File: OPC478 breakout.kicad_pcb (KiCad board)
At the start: 2 copper layers, 26 x 29.8 mm, 14 parts, among them J1 Conn_01x05_Pin, J2 AudioPlug4, Q1 BC557, Q2 BC547

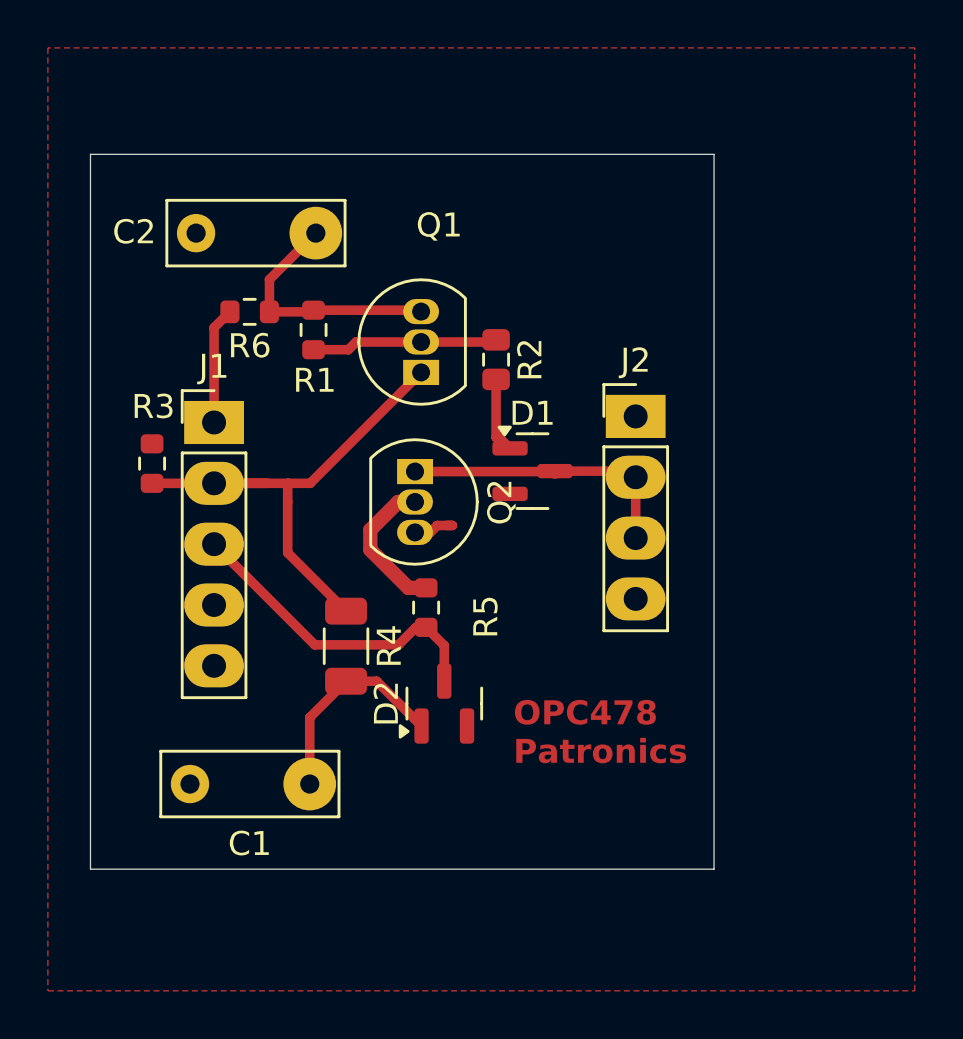
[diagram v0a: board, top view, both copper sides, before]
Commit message: adjust component layers to better match physical assembly
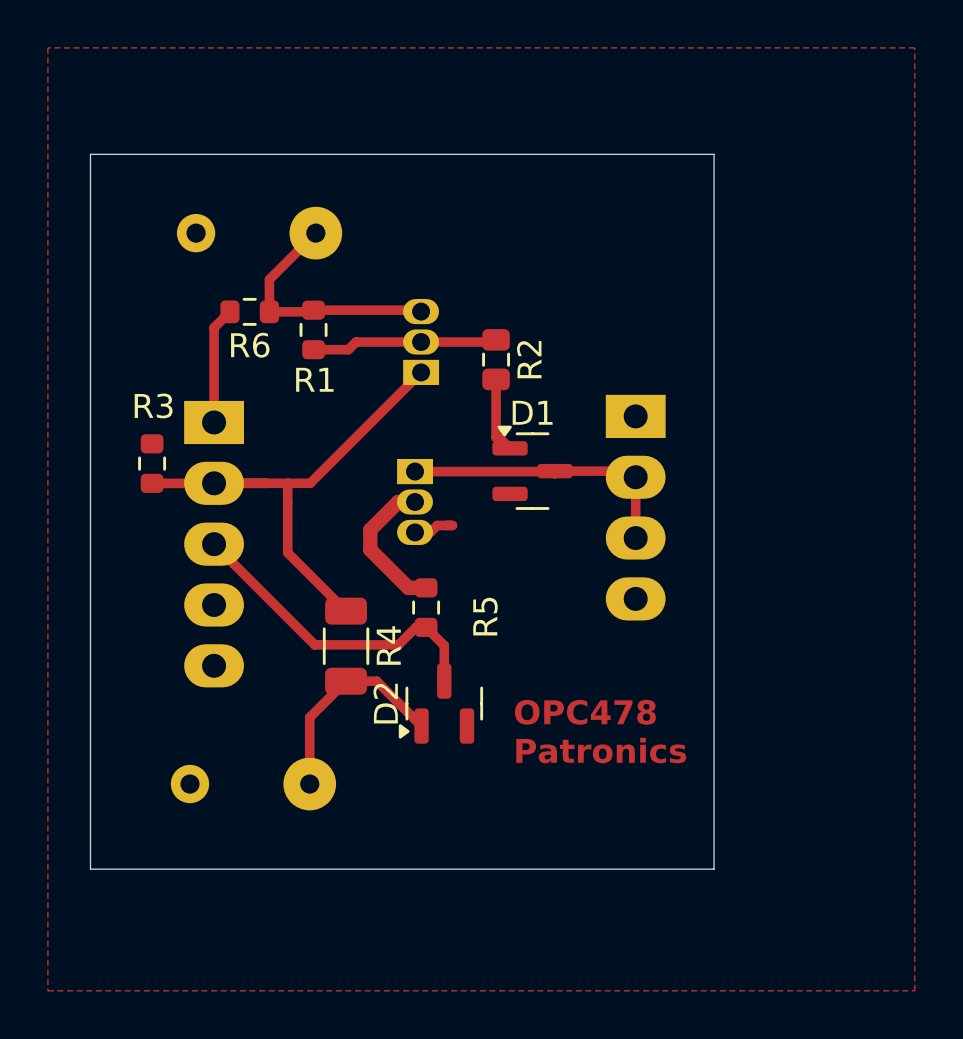
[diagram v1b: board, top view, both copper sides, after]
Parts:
- C1, C2, J1, J2, Q1, Q2: moved to B.Cu
- turned J1 to 180 degrees
- turned J2 to 180 degrees

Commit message: further widen pads and traces to improve ease of milling and soldering
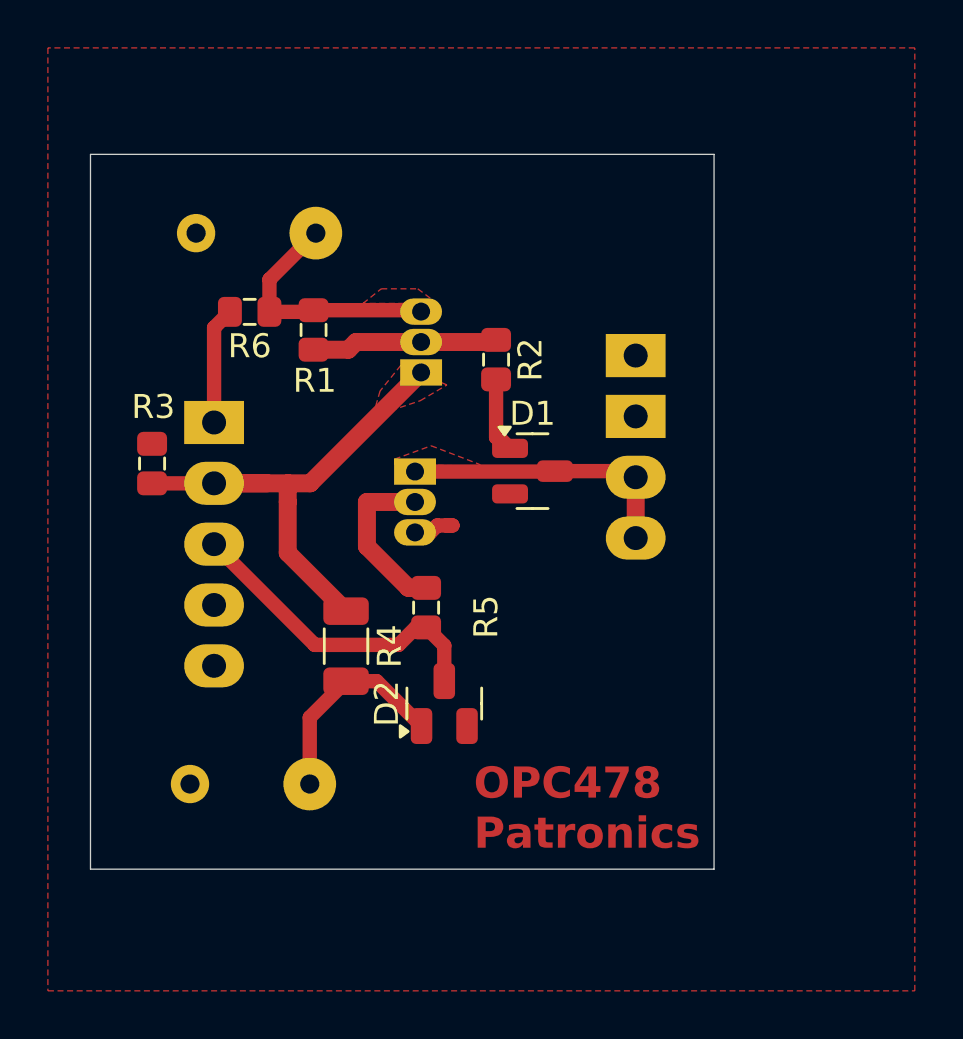
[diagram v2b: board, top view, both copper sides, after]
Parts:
- moved J2 2.54 mm to (121.8, 76.3)
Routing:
- net Net-(Q2-B): track 6.17 -> 7.05 mm
- added copper zone on F.Cu, net Net-(D1-K)
- added copper zone on F.Cu, net Net-(J1-Pin_2)
- added copper zone on F.Cu, net Net-(Q1-E)
